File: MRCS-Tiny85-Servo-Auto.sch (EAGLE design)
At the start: 14 parts, among them U1 ATTINY85-20PU

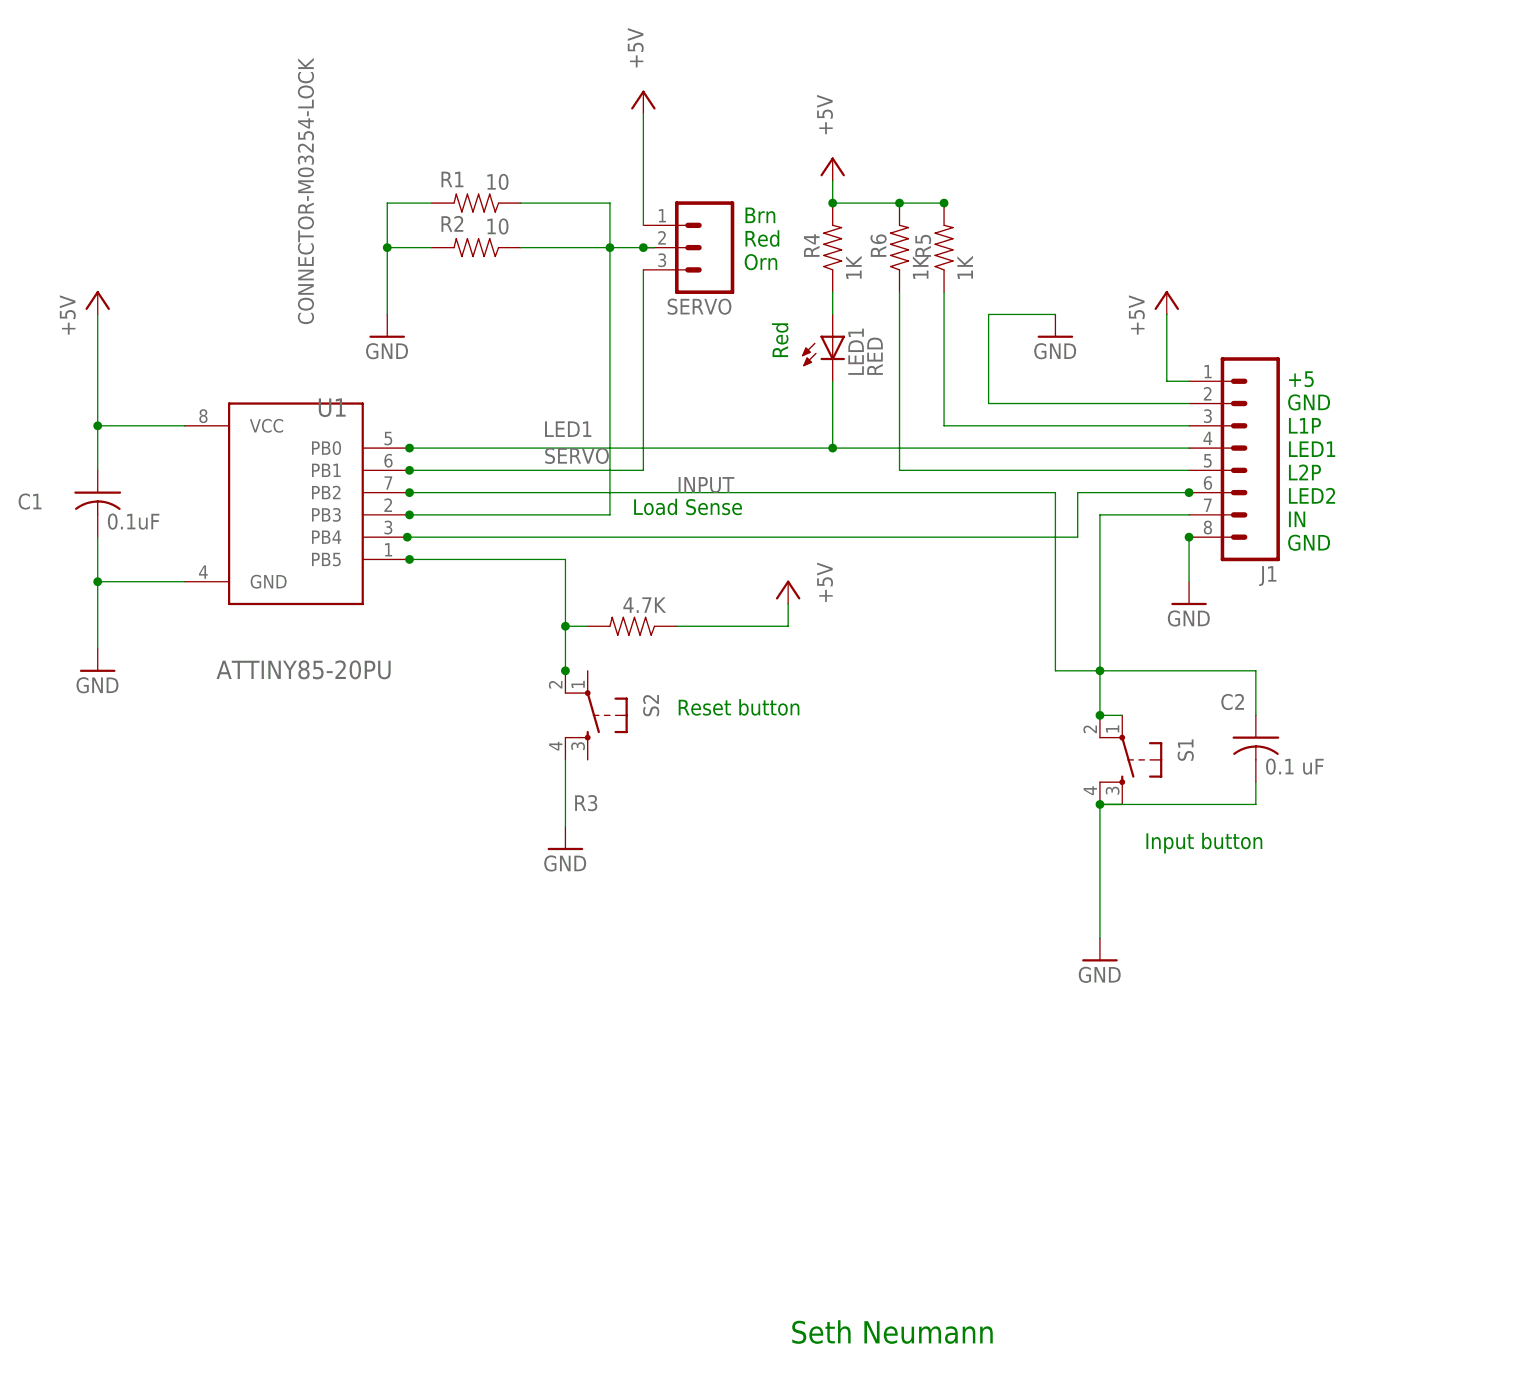
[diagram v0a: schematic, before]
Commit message: Moved one of the push buttons away from socket
This makes it easier to remove the ATTiny for reprogramming
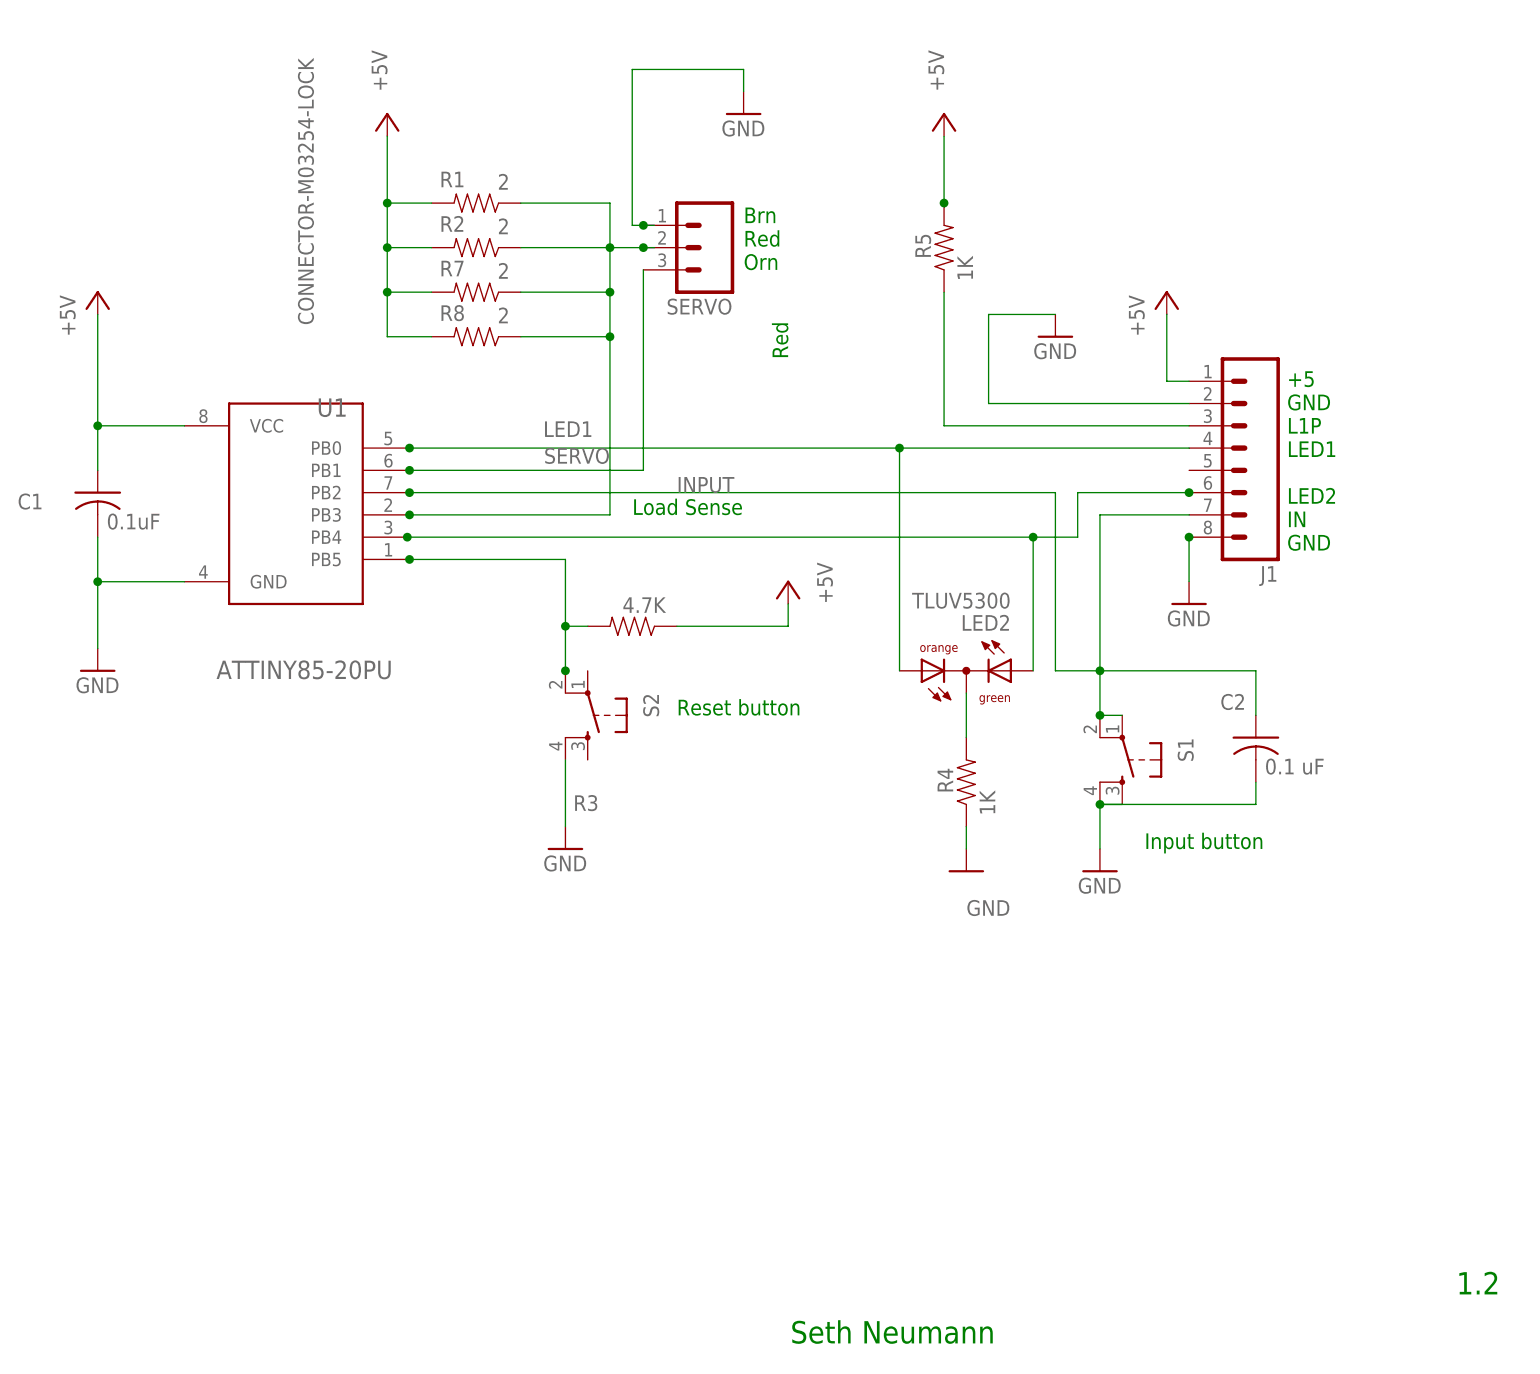
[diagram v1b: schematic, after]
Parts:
- removed LED1: RED, SPCoast:LEDLED3MM
- removed R6: 1K, SPCoast:RPTH04
- added LED2: TLUV5300, led:TLUV5300
- added R7, R8: 2, SPCoast:RPTH04
- R1, R2: value 10 -> 2
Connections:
- removed net LED2PWR: J1.5, R6.1
- removed net N$2: LED1.A, R4.1
- new net N$1: LED2.CC, R4.2
- net +5V: now also R1.2, R2.2, R7.2, R8.2; no longer R4.2, R6.2, SERVO.1
- net ADC3: now also R7.1, R8.1
- net GND: now also R4.1, SERVO.1; no longer R1.2, R2.2
- net LED1: now also LED2.AO; no longer LED1.C
- net N$4: now also LED2.AG
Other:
- note added: "+5 GND L1P LED1 LED2 IN GND"
- note added: "1.2"
- note removed: "+5 GND L1P LED1 L2P LED2 IN GND"
- moved on the sheet: R4
